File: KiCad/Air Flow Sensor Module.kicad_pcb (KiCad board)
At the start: 2 copper layers, 39.4 x 62.2 mm, 18 parts, among them Q1 TIP122, U1 LM358, U2 4N32

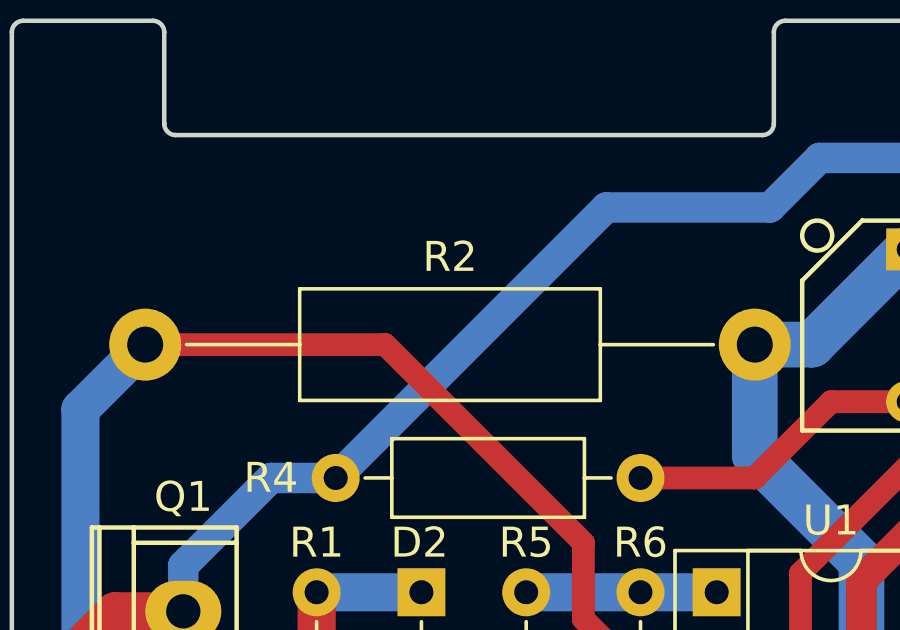
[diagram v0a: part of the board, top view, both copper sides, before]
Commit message: Replaced component R2 footprint to allow for resistor size of proper wattage
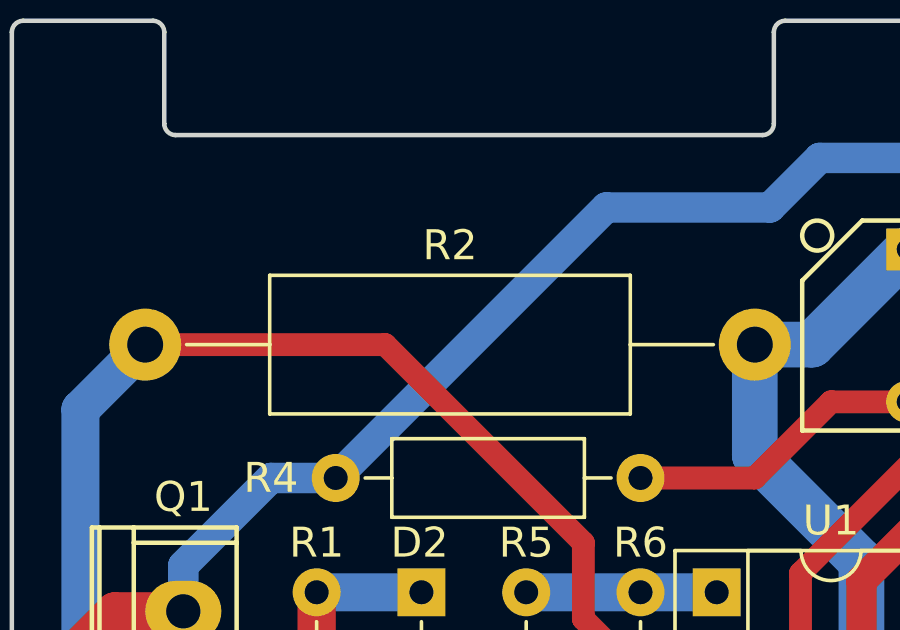
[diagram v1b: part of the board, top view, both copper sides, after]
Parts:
- R2: footprint Resistors_THT:R_Axial_DIN0411_L9.9mm_D3.6mm_P20.32mm_Horizontal -> Resistors_THT:R_Axial_DIN0414_L11.9mm_D4.5mm_P20.32mm_Horizontal
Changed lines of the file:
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@@
-    )
-  )
-  (module Resistors_THT:R_Axial_DIN0411_L9.9mm_D3.6mm_P20.32mm_Horizontal (layer F.Cu)
-    (at 133.35 84.455)
-    (descr "Resistor, Axial_DIN0411 series, Axial, Horizontal, pin pitch=20.32mm, 1W = 1/1W, length*diameter=9.9*3.6mm^2")
-    (tags "Resistor Axial_DIN0411 series Axial Horizontal pin pitch 20.32mm 1W = 1/1W length 9.9mm diameter 3.6mm")
-    (fp_text reference R2 (at 10.16 -2.921) (layer F.SilkS)
-      (effects (font (size 1 1) (thickness 0.15)))
-    )
-    (fp_text value 68R (at 10.16 2.86) (layer F.Fab)
-      (effects (font (size 1 1) (thickness 0.15)))
-    )
-    (fp_line (start 5.21 -1.8) (end 5.21 1.8) (layer F.Fab) (width 0.1))
-    (fp_line (start 5.21 1.8) (end 15.11 1.8) (layer F.Fab) (width 0.1))
-    (fp_line (start 15.11 1.8) (end 15.11 -1.8) (layer F.Fab) (width 0.1))
-    (fp_line (start 15.11 -1.8) (end 5.21 -1.8) (layer F.Fab) (width 0.1))
-    (fp_line (start 0 0) (end 5.21 0) (layer F.Fab) (width 0.1))
-    (fp_line (start 20.32 0) (end 15.11 0) (layer F.Fab) (width 0.1))
-    (fp_line (start 5.15 -1.86) (end 5.15 1.86) (layer F.SilkS) (width 0.12))
-    (fp_line (start 5.15 1.86) (end 15.17 1.86) (layer F.SilkS) (width 0.12))
-    (fp_line (start 15.17 1.86) (end 15.17 -1.86) (layer F.SilkS) (width 0.12))
-    (fp_line (start 15.17 -1.86) (end 5.15 -1.86) (layer F.SilkS) (width 0.12))
-    (fp_line (start 1.38 0) (end 5.15 0) (layer F.SilkS) (width 0.12))
-    (fp_line (start 18.94 0) (end 15.17 0) (layer F.SilkS) (width 0.12))
-    (fp_line (start -1.45 -2.15) (end -1.45 2.15) (layer F.CrtYd) (width 0.05))
-    (fp_line (start -1.45 2.15) (end 21.8 2.15) (layer F.CrtYd) (width 0.05))
-    (fp_line (start 21.8 2.15) (end 21.8 -2.15) (layer F.CrtYd) (width 0.05))
-    (fp_line (start 21.8 -2.15) (end -1.45 -2.15) (layer F.CrtYd) (width 0.05))
-    (pad 1 thru_hole circle (at 0 0) (size 2.4 2.4) (drill 1.2) (layers *.Cu *.Mask)
-      (net 9 "Net-(R2-Pad1)"))
-    (pad 2 thru_hole oval (at 20.32 0) (size 2.4 2.4) (drill 1.2) (layers *.Cu *.Mask)
-      (net 4 IN2))
-    (model Resistors_ThroughHole.3dshapes/R_Axial_DIN0411_L9.9mm_D3.6mm_P20.32mm_Horizontal.wrl
-      (at (xyz 0 0 0))
-      (scale (xyz 0.393701 0.393701 0.393701))
-      (rotate (xyz 0 0 0))
     )
   )
@@
       (net 10 "Net-(R3-Pad2)"))
   )
+  (module Resistors_THT:R_Axial_DIN0414_L11.9mm_D4.5mm_P20.32mm_Horizontal (layer F.Cu)
+    (at 133.35 84.455)
+    (descr "Resistor, Axial_DIN0414 series, Axial, Horizontal, pin pitch=20.32mm, 2W, length*diameter=11.9*4.5mm^2, http://www.vishay.com/docs/20128/wkxwrx.pdf")
+    (tags "Resistor Axial_DIN0414 series Axial Horizontal pin pitch 20.32mm 2W length 11.9mm diameter 4.5mm")
+    (fp_text reference R2 (at 10.16 -3.31) (layer F.SilkS)
+      (effects (font (size 1 1) (thickness 0.15)))
+    )
+    (fp_text value 68R (at 10.16 3.31) (layer F.Fab)
+      (effects (font (size 1 1) (thickness 0.15)))
+    )
+    (fp_line (start 4.21 -2.25) (end 4.21 2.25) (layer F.Fab) (width 0.1))
+    (fp_line (start 4.21 2.25) (end 16.11 2.25) (layer F.Fab) (width 0.1))
+    (fp_line (start 16.11 2.25) (end 16.11 -2.25) (layer F.Fab) (width 0.1))
+    (fp_line (start 16.11 -2.25) (end 4.21 -2.25) (layer F.Fab) (width 0.1))
+    (fp_line (start 0 0) (end 4.21 0) (layer F.Fab) (width 0.1))
+    (fp_line (start 20.32 0) (end 16.11 0) (layer F.Fab) (width 0.1))
+    (fp_line (start 4.15 -2.31) (end 4.15 2.31) (layer F.SilkS) (width 0.12))
+    (fp_line (start 4.15 2.31) (end 16.17 2.31) (layer F.SilkS) (width 0.12))
+    (fp_line (start 16.17 2.31) (end 16.17 -2.31) (layer F.SilkS) (width 0.12))
+    (fp_line (start 16.17 -2.31) (end 4.15 -2.31) (layer F.SilkS) (width 0.12))
+    (fp_line (start 1.38 0) (end 4.15 0) (layer F.SilkS) (width 0.12))
+    (fp_line (start 18.94 0) (end 16.17 0) (layer F.SilkS) (width 0.12))
+    (fp_line (start -1.45 -2.6) (end -1.45 2.6) (layer F.CrtYd) (width 0.05))
+    (fp_line (start -1.45 2.6) (end 21.8 2.6) (layer F.CrtYd) (width 0.05))
+    (fp_line (start 21.8 2.6) (end 21.8 -2.6) (layer F.CrtYd) (width 0.05))
+    (fp_line (start 21.8 -2.6) (end -1.45 -2.6) (layer F.CrtYd) (width 0.05))
+    (pad 1 thru_hole circle (at 0 0) (size 2.4 2.4) (drill 1.2) (layers *.Cu *.Mask)
+      (net 9 "Net-(R2-Pad1)"))
+    (pad 2 thru_hole oval (at 20.32 0) (size 2.4 2.4) (drill 1.2) (layers *.Cu *.Mask)
+      (net 4 IN2))
+    (model Resistors_THT.3dshapes/R_Axial_DIN0414_L11.9mm_D4.5mm_P20.32mm_Horizontal.wrl
+      (at (xyz 0 0 0))
+      (scale (xyz 0.393701 0.393701 0.393701))
+      (rotate (xyz 0 0 0))
+    )
+  )
   (gr_text "A replica of the optional air flow sensor module for use with the high voltage DC power\nsupply in Trion HE Plus 1400 and HE Plus 2000 electronic air cleaners circa 2005.  Later\nrevisions of the power supply have this module integrated into the main PCB." (at 177.8 170.18) (layer Cmts.User)

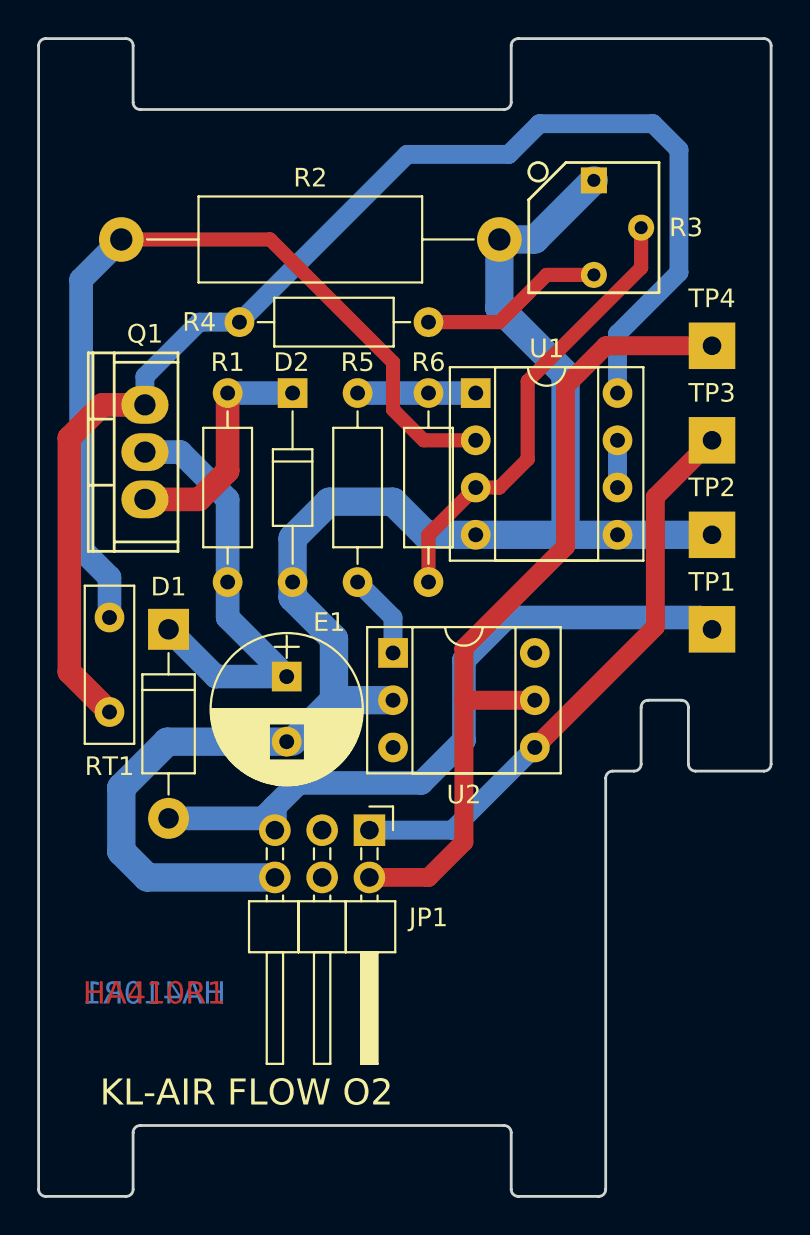
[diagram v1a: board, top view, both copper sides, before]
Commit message: Adjusted traces beneath components U1 and U2 to more closely match original
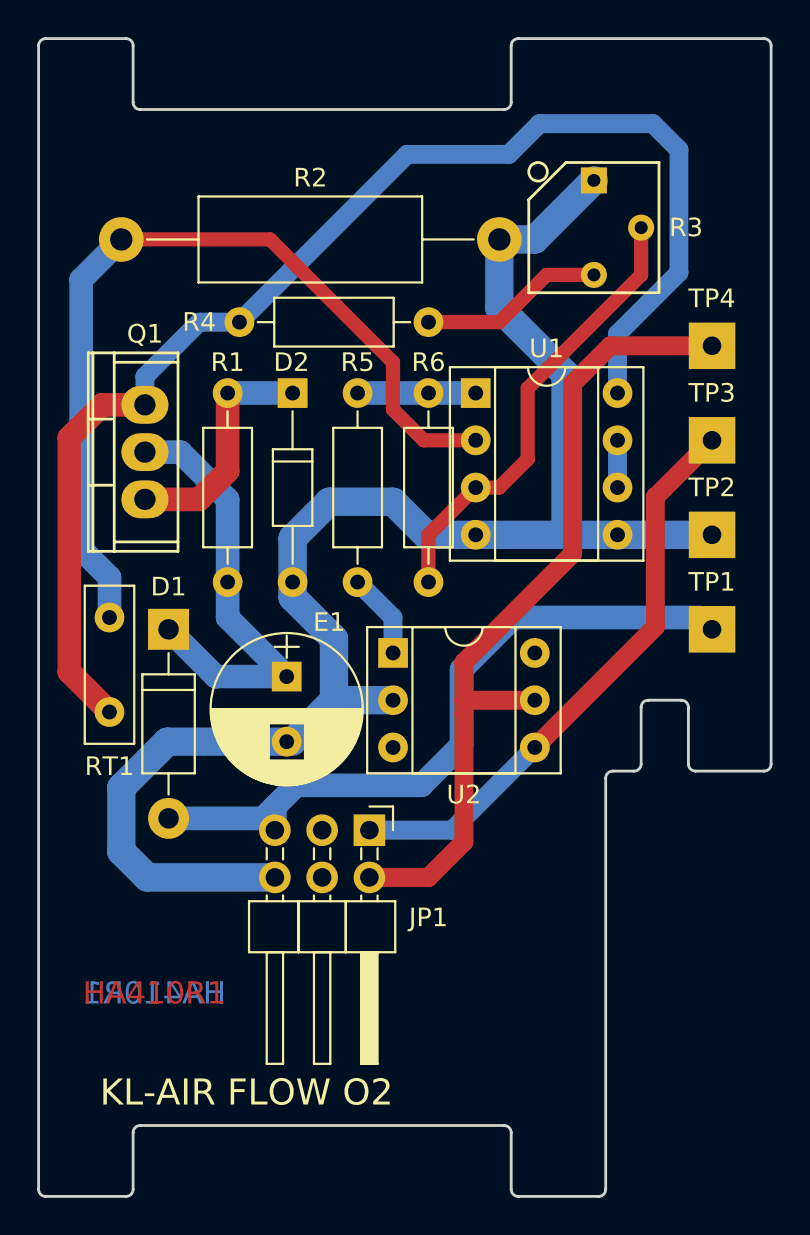
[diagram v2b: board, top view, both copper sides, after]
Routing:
- net IN1: track 37.7 -> 36.7 mm
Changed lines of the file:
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@@
   (segment (start 136.525 95.885) (end 139.065 98.425) (width 1.27) (layer B.Cu) (net 1))
   (segment (start 139.065 98.425) (end 139.065 102.87) (width 1.27) (layer B.Cu) (net 1) (status 20))
-  (segment (start 164.465 104.775) (end 154.051 104.775) (width 1.27) (layer B.Cu) (net 2) (status 10))
-  (segment (start 151.765 107.061) (end 151.765 111.379) (width 1.27) (layer B.Cu) (net 2))
-  (segment (start 154.051 104.775) (end 151.765 107.061) (width 1.27) (layer B.Cu) (net 2))
-  (segment (start 142.875 113.665) (end 149.479 113.665) (width 1.27) (layer B.Cu) (net 2))
-  (segment (start 149.479 113.665) (end 151.765 111.379) (width 1.27) (layer B.Cu) (net 2))
-  (segment (start 141.605 114.935) (end 142.875 113.665) (width 1.27) (layer B.Cu) (net 2))
+  (segment (start 149.479 113.792) (end 151.638 111.633) (width 1.27) (layer B.Cu) (net 2))
+  (segment (start 142.748 113.792) (end 149.479 113.792) (width 1.27) (layer B.Cu) (net 2))
+  (segment (start 151.638 107.569) (end 154.432 104.775) (width 1.27) (layer B.Cu) (net 2))
+  (segment (start 151.638 111.633) (end 151.638 107.569) (width 1.27) (layer B.Cu) (net 2))
+  (segment (start 164.465 104.775) (end 154.432 104.775) (width 1.27) (layer B.Cu) (net 2))
+  (segment (start 142.748 113.792) (end 141.605 114.935) (width 1.27) (layer B.Cu) (net 2))
   (segment (start 141.605 114.935) (end 141.605 116.205) (width 1.27) (layer B.Cu) (net 2) (status 20))
   (segment (start 140.97 115.57) (end 135.89 115.57) (width 1.27) (layer B.Cu) (net 2) (status 20))
   (segment (start 141.605 114.935) (end 140.97 115.57) (width 1.27) (layer B.Cu) (net 2))
-  (segment (start 164.465 104.775) (end 165.1 105.41) (width 1.27) (layer B.Cu) (net 2) (status 30))
   (segment (start 134.62 98.425) (end 137.541 98.425) (width 1.27) (layer F.Cu) (net 3) (status 10))
   (segment (start 139.065 96.901) (end 139.065 92.71) (width 1.27) (layer F.Cu) (net 3) (status 20))
@@
   (segment (start 146.685 116.205) (end 151.13 116.205) (width 1.016) (layer B.Cu) (net 5) (status 10))
   (segment (start 151.13 116.205) (end 155.575 111.76) (width 1.016) (layer B.Cu) (net 5) (status 20))
-  (segment (start 151.765 106.426) (end 157.226 100.965) (width 1.016) (layer F.Cu) (net 6))
-  (segment (start 165.1 90.17) (end 159.385 90.17) (width 1.016) (layer F.Cu) (net 6))
-  (segment (start 151.765 106.426) (end 151.765 109.22) (width 1.016) (layer F.Cu) (net 6))
-  (segment (start 157.226 92.329) (end 159.385 90.17) (width 1.016) (layer F.Cu) (net 6))
-  (segment (start 157.226 100.965) (end 157.226 92.329) (width 1.016) (layer F.Cu) (net 6))
+  (segment (start 157.607 92.202) (end 159.639 90.17) (width 1.016) (layer F.Cu) (net 6))
+  (segment (start 157.607 101.346) (end 157.607 92.202) (width 1.016) (layer F.Cu) (net 6))
+  (segment (start 157.607 101.346) (end 151.765 107.188) (width 1.016) (layer F.Cu) (net 6))
+  (segment (start 151.765 109.22) (end 151.765 107.188) (width 1.016) (layer F.Cu) (net 6))
+  (segment (start 159.639 90.17) (end 165.1 90.17) (width 1.016) (layer F.Cu) (net 6))
   (segment (start 155.575 109.22) (end 151.765 109.22) (width 1.016) (layer F.Cu) (net 6) (status 10))
-  (segment (start 151.765 109.22) (end 151.765 116.84) (width 1.016) (layer F.Cu) (net 6))
+  (segment (start 151.765 109.22) (end 151.765 109.982) (width 1.016) (layer F.Cu) (net 6))
+  (segment (start 151.765 109.982) (end 151.765 116.84) (width 1.016) (layer F.Cu) (net 6))
   (segment (start 146.685 118.745) (end 149.86 118.745) (width 1.016) (layer F.Cu) (net 6) (status 10))
   (segment (start 149.86 118.745) (end 151.765 116.84) (width 1.016) (layer F.Cu) (net 6))
@@
   (segment (start 131.191 101.092) (end 132.715 102.616) (width 1.27) (layer B.Cu) (net 9))
   (segment (start 132.715 102.616) (end 132.715 104.775) (width 1.27) (layer B.Cu) (net 9) (status 20))
-  (segment (start 155.194 92.075) (end 155.194 96.266) (width 0.762) (layer F.Cu) (net 10))
-  (segment (start 161.29 83.82) (end 161.29 85.979) (width 0.762) (layer F.Cu) (net 10))
-  (segment (start 155.194 92.075) (end 161.29 85.979) (width 0.762) (layer F.Cu) (net 10))
+  (segment (start 155.194 92.456) (end 161.29 86.36) (width 0.762) (layer F.Cu) (net 10))
   (segment (start 153.67 97.79) (end 155.194 96.266) (width 0.762) (layer F.Cu) (net 10))
-  (segment (start 153.67 97.79) (end 152.4 97.79) (width 0.762) (layer F.Cu) (net 10) (status 10))
+  (segment (start 152.4 97.79) (end 153.67 97.79) (width 0.762) (layer F.Cu) (net 10) (status 10))
+  (segment (start 155.194 96.266) (end 155.194 92.456) (width 0.762) (layer F.Cu) (net 10))
+  (segment (start 161.29 86.36) (end 161.29 83.82) (width 0.762) (layer F.Cu) (net 10))
   (segment (start 149.86 102.87) (end 149.86 100.33) (width 0.762) (layer F.Cu) (net 10) (status 10))
   (segment (start 149.86 100.33) (end 152.4 97.79) (width 0.762) (layer F.Cu) (net 10) (status 20))
